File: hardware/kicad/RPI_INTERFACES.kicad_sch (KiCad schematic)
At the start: 0 parts

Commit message: feat: mcu interfaces & motor connections
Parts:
- added J2: Conn_02x20_Counter_Clockwise_MountingPin, Connector_Hirose_DF40:Hirose_DF40C-40DS-0.4V_2x20_P0.4mm, symbol Connector_Generic_MountingPin:Conn_02x20_Counter_Clockwise_MountingPin
- added R1, R5, R6, R7, R8: R, symbol Device:R
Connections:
- new net GND_LOGIC: J2.6 (Pin_6)
- new net GPIO10: J2.19 (Pin_19), R6.1
- new net GPIO11: J2.23 (Pin_23), R1.1
- new net GPIO25: J2.22 (Pin_22), R8.1
- new net GPIO8: J2.24 (Pin_24), R7.1
- new net GPIO9: J2.21 (Pin_21), R5.1
- new net MCU_INT: R8.2
- new net SPI_CS: R7.2
- new net SPI_MISO: R5.2
- new net SPI_MOSI: R6.2
- new net SPI_SCK: R1.2

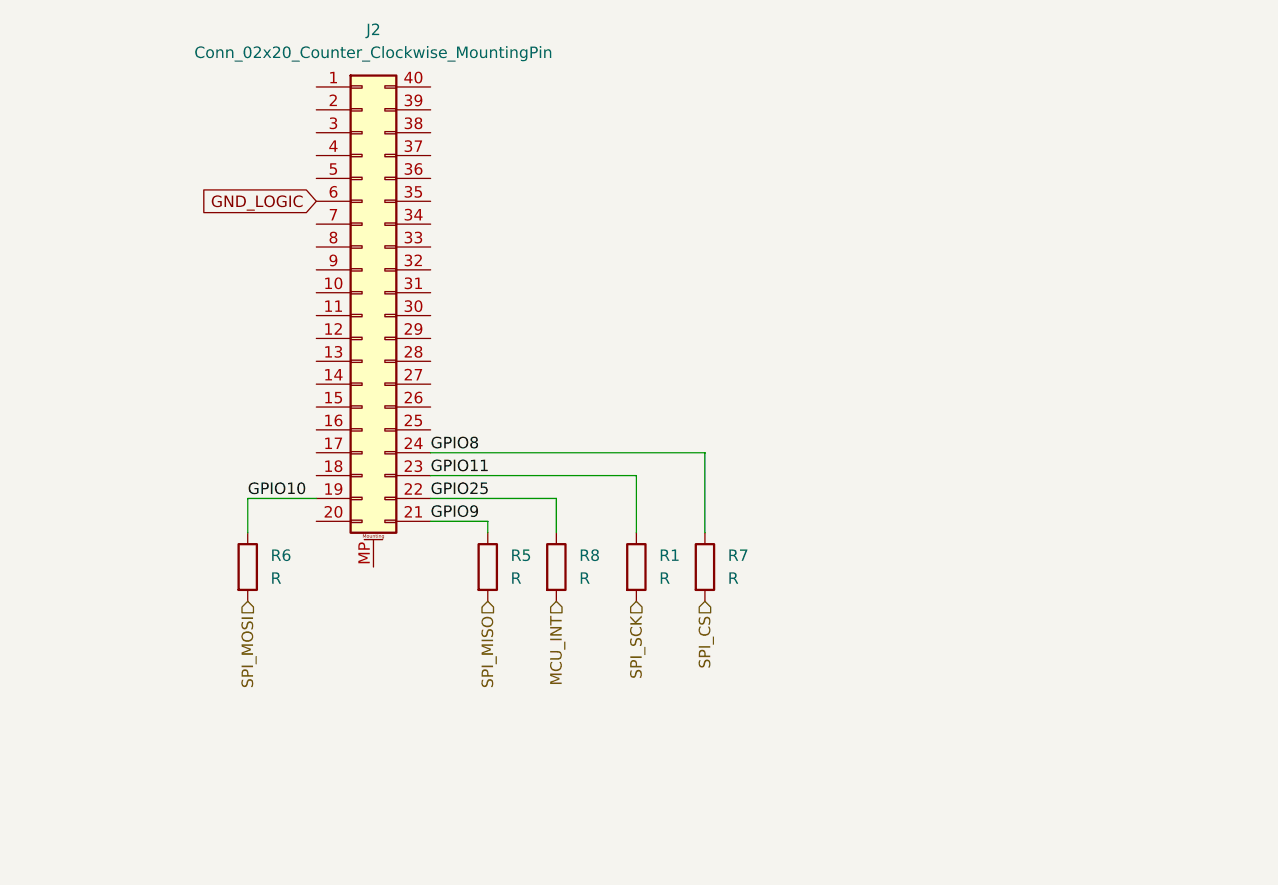
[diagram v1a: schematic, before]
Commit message: feat: implemented keypad & reverse polarity protection
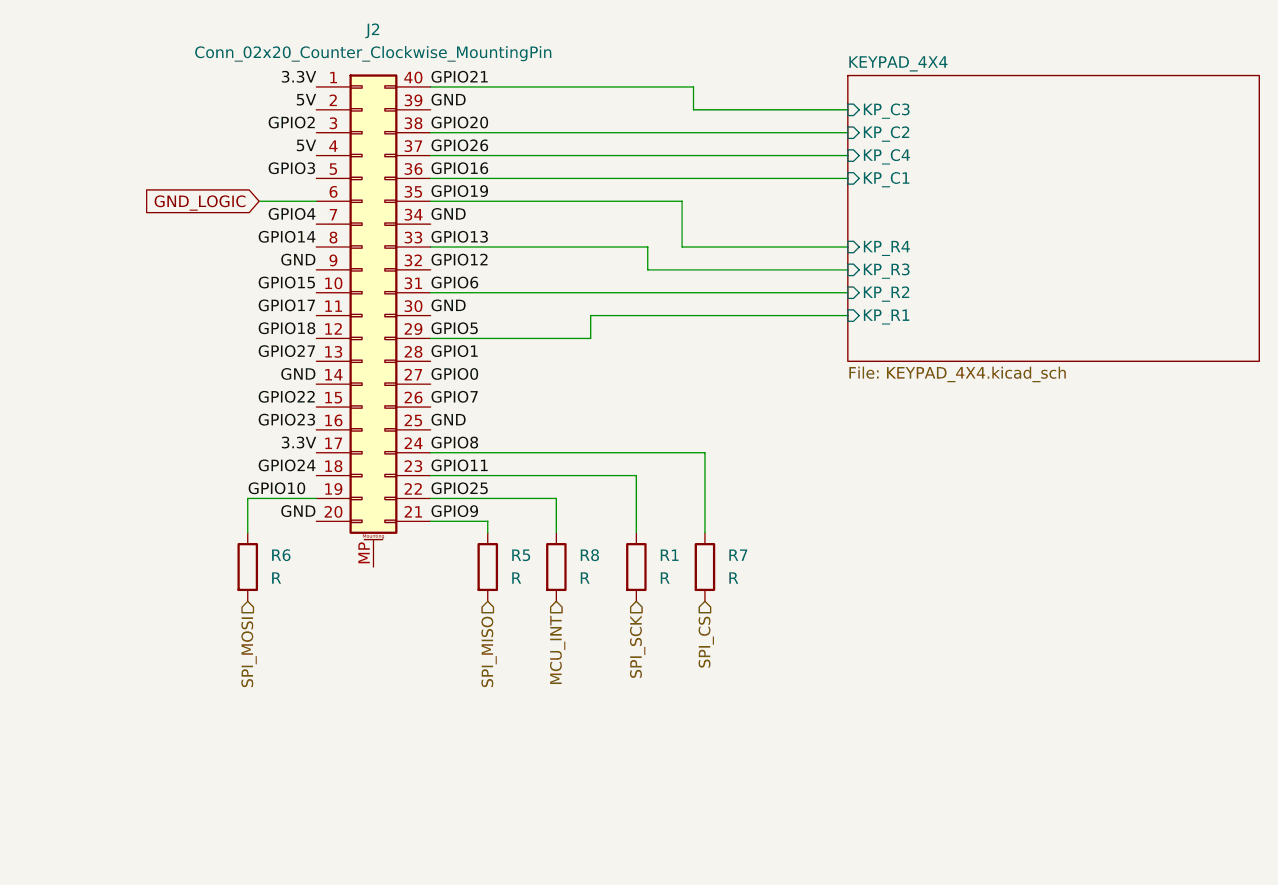
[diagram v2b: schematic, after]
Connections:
- net 3.3V: now reaches J2.1 (Pin_1)
- net 3.3V: now also J2.17 (Pin_17)
- net GPIO15: now reaches J2.10 (Pin_10)
- net GPIO17: now reaches J2.11 (Pin_11)
- net GPIO18: now reaches J2.12 (Pin_12)
- net GPIO27: now reaches J2.13 (Pin_13)
- net GND: now reaches J2.14 (Pin_14)
- net GND: now also J2.20 (Pin_20), J2.25 (Pin_25), J2.30 (Pin_30), J2.34 (Pin_34), J2.39 (Pin_39), J2.9 (Pin_9)
- net GPIO22: now reaches J2.15 (Pin_15)
- net GPIO23: now reaches J2.16 (Pin_16)
- net GPIO24: now reaches J2.18 (Pin_18)
- net 5V: now reaches J2.2 (Pin_2)
- net 5V: now also J2.4 (Pin_4)
- net GPIO7: now reaches J2.26 (Pin_26)
- net GPIO0: now reaches J2.27 (Pin_27)
- net GPIO1: now reaches J2.28 (Pin_28)
- net GPIO5: now reaches J2.29 (Pin_29)
- net GPIO2: now reaches J2.3 (Pin_3)
- net GPIO6: now reaches J2.31 (Pin_31)
- net GPIO12: now reaches J2.32 (Pin_32)
- net GPIO13: now reaches J2.33 (Pin_33)
- net GPIO19: now reaches J2.35 (Pin_35)
- net GPIO16: now reaches J2.36 (Pin_36)
- net GPIO26: now reaches J2.37 (Pin_37)
- net GPIO20: now reaches J2.38 (Pin_38)
- net GPIO21: now reaches J2.40 (Pin_40)
- net GPIO3: now reaches J2.5 (Pin_5)
- net GPIO4: now reaches J2.7 (Pin_7)
- net GPIO14: now reaches J2.8 (Pin_8)
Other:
- added sheet KEYPAD_4X4 (KEYPAD_4X4.kicad_sch)

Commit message: fix: error fixing & connection config
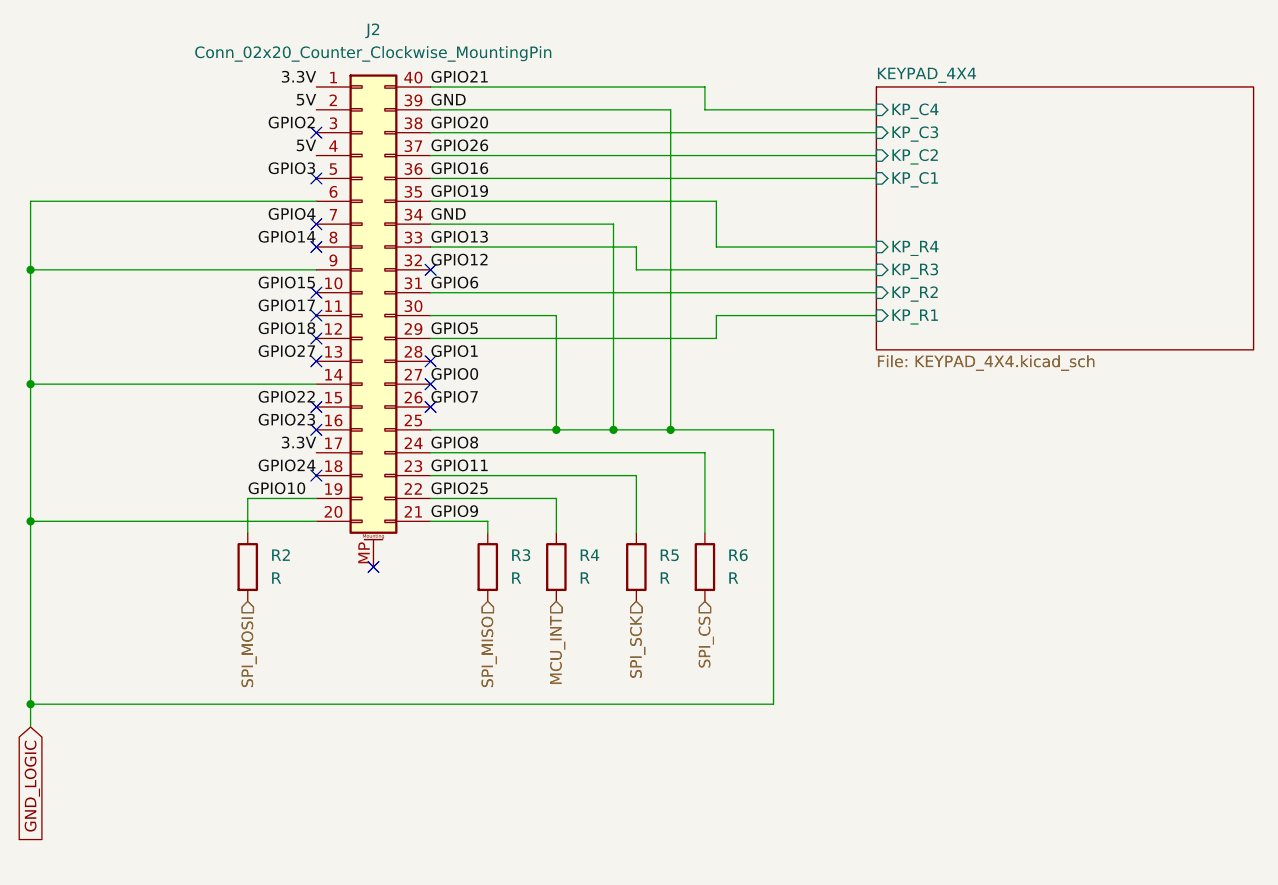
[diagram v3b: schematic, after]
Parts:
- renumbered R6 to R2, R5 to R3, R8 to R4, R1 to R5, R7 to R6
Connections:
- net GND is gone; now on net GND_LOGIC: J2.14 (Pin_14), J2.20 (Pin_20), J2.25 (Pin_25), J2.30 (Pin_30), J2.34 (Pin_34), J2.39 (Pin_39), J2.9 (Pin_9)
- no-connect marks 0 -> 16

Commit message: docs: added end semester report for project
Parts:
- J2: symbol Connector_Generic_MountingPin:Conn_02x20_Counter_Clockwise_MountingPin -> TPSM82903:Conn_02x20_Counter_Clockwise_MountingPin
- R2, R3, R4, R5, R6: symbol Device:R -> TPSM82903:R
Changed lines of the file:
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@@
 	)
 	(symbol
-		(lib_id "Device:R")
+		(lib_id "TPSM82903:R")
 		(at 105.41 119.38 0)
 		(unit 1)
@@
 	)
 	(symbol
-		(lib_id "Device:R")
+		(lib_id "TPSM82903:R")
 		(at 121.92 119.38 0)
 		(unit 1)
@@
 	)
 	(symbol
-		(lib_id "Connector_Generic_MountingPin:Conn_02x20_Counter_Clockwise_MountingPin")
+		(lib_id "TPSM82903:Conn_02x20_Counter_Clockwise_MountingPin")
 		(at 91.44 88.9 0)
 		(unit 1)
@@
 	)
 	(symbol
-		(lib_id "Device:R")
+		(lib_id "TPSM82903:R")
 		(at 113.03 119.38 0)
 		(unit 1)
@@
 	)
 	(symbol
-		(lib_id "Device:R")
+		(lib_id "TPSM82903:R")
 		(at 129.54 119.38 0)
 		(unit 1)
@@
 	)
 	(symbol
-		(lib_id "Device:R")
+		(lib_id "TPSM82903:R")
 		(at 78.74 119.38 0)
 		(unit 1)
